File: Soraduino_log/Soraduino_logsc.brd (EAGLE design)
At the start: 27.4 x 29.5 mm, 26 parts, among them IC1 ATMEGA168-AU, IC2 LM1117IMPX-3.3, IC3 LM1117MPX-5.0

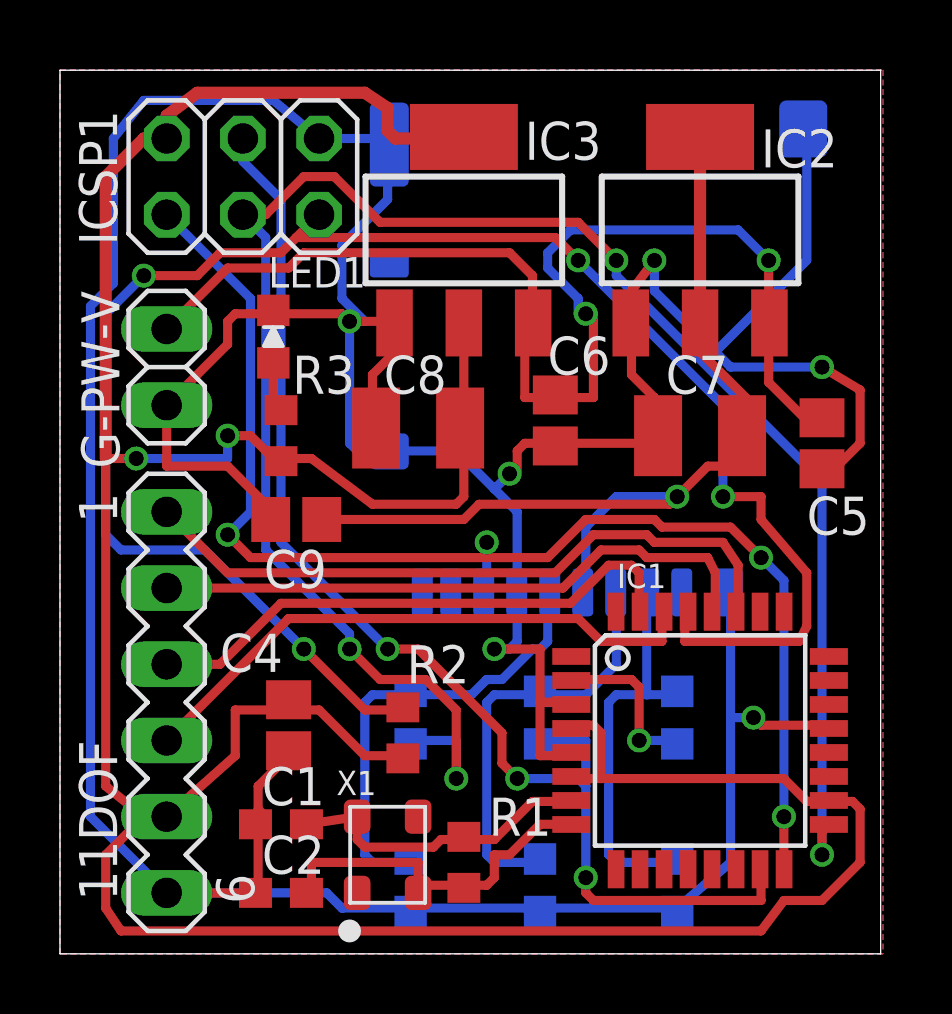
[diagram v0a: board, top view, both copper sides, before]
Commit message: fix I2C port mistake about sch
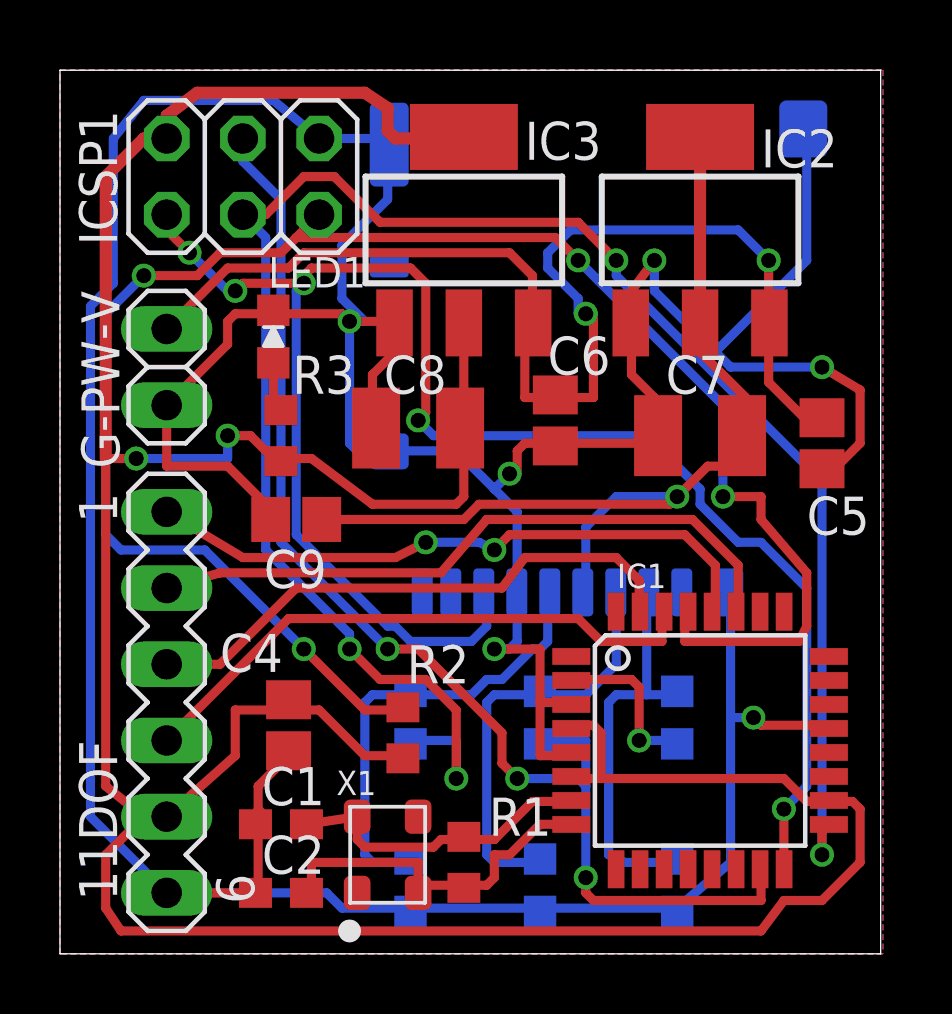
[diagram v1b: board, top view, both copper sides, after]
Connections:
- removed net N$9: 11DOF.2, IC1.28
- new net N$3: 11DOF.1, IC1.28
- net N$8: now also 11DOF.2; no longer 11DOF.1
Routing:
- net N$3: track 0.00 -> 21.2 mm, vias 0 -> 2
- net N$9: track 20.6 -> 0.00 mm
- net N$15: track 44.2 -> 58.4 mm, vias 4 -> 5
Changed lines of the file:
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@@
 <?xml version="1.0" encoding="utf-8"?>
 <!DOCTYPE eagle SYSTEM "eagle.dtd">
-<eagle version="6.4">
+<eagle version="6.5.0">
 <drawing>
 <settings>
@@
 <signal name="N$8">
 <contactref element="IC1" pad="27"/>
-<contactref element="11DOF" pad="1"/>
+<contactref element="11DOF" pad="2"/>
 <wire x1="22.606" y1="12.954" x2="22.606" y2="11.43" width="0.3048" layer="1"/>
-<wire x1="22.098" y1="13.716" x2="22.606" y2="12.954" width="0.3048" layer="1"/>
-<wire x1="19.812" y1="13.716" x2="22.098" y2="13.716" width="0.3048" layer="1"/>
-<wire x1="19.558" y1="13.97" x2="19.812" y2="13.716" width="0.3048" layer="1"/>
-<wire x1="17.78" y1="13.97" x2="19.558" y2="13.97" width="0.3048" layer="1"/>
-<wire x1="16.51" y1="12.7" x2="17.78" y2="13.97" width="0.3048" layer="1"/>
-<wire x1="5.588" y1="12.7" x2="16.51" y2="12.7" width="0.3048" layer="1"/>
-<wire x1="3.556" y1="14.732" x2="5.588" y2="12.7" width="0.3048" layer="1"/>
+<wire x1="21.082" y1="14.478" x2="22.606" y2="12.954" width="0.3048" layer="1"/>
+<wire x1="14.224" y1="14.478" x2="21.082" y2="14.478" width="0.3048" layer="1"/>
+<wire x1="12.7" y1="12.7" x2="14.224" y2="14.478" width="0.3048" layer="1"/>
+<wire x1="5.334" y1="12.7" x2="12.7" y2="12.7" width="0.3048" layer="1"/>
+<wire x1="3.556" y1="12.192" x2="5.334" y2="12.7" width="0.3048" layer="1"/>
 <wire x1="22.606" y1="11.43" x2="22.536" y2="11.4046" width="0.3048" layer="1"/>
-</signal>
-<signal name="N$9">
-<contactref element="IC1" pad="28"/>
-<contactref element="11DOF" pad="2"/>
-<wire x1="21.844" y1="12.7" x2="21.844" y2="11.43" width="0.3048" layer="1"/>
-<wire x1="21.59" y1="13.208" x2="21.844" y2="12.7" width="0.3048" layer="1"/>
-<wire x1="19.558" y1="13.208" x2="21.59" y2="13.208" width="0.3048" layer="1"/>
-<wire x1="19.304" y1="13.462" x2="19.558" y2="13.208" width="0.3048" layer="1"/>
-<wire x1="18.034" y1="13.462" x2="19.304" y2="13.462" width="0.3048" layer="1"/>
-<wire x1="16.764" y1="12.192" x2="18.034" y2="13.462" width="0.3048" layer="1"/>
-<wire x1="3.556" y1="12.192" x2="16.764" y2="12.192" width="0.3048" layer="1"/>
-<wire x1="21.844" y1="11.43" x2="21.736" y2="11.4046" width="0.3048" layer="1"/>
 </signal>
 <signal name="+5V">
@@
 <contactref element="U$1" pad="7"/>
 <contactref element="ICSP1" pad="1"/>
-<wire x1="24.13" y1="4.572" x2="24.13" y2="3.048" width="0.3048" layer="1"/>
-<wire x1="24.13" y1="12.446" x2="24.13" y2="4.572" width="0.3048" layer="16"/>
-<wire x1="23.368" y1="13.208" x2="24.13" y2="12.446" width="0.3048" layer="16"/>
-<wire x1="22.352" y1="14.224" x2="23.368" y2="13.208" width="0.3048" layer="1"/>
-<wire x1="20.066" y1="14.224" x2="22.352" y2="14.224" width="0.3048" layer="1"/>
-<wire x1="19.812" y1="14.478" x2="20.066" y2="14.224" width="0.3048" layer="1"/>
-<wire x1="17.526" y1="14.478" x2="19.812" y2="14.478" width="0.3048" layer="1"/>
-<wire x1="16.256" y1="13.208" x2="17.526" y2="14.478" width="0.3048" layer="1"/>
-<wire x1="6.35" y1="13.208" x2="14.224" y2="13.208" width="0.3048" layer="1"/>
-<wire x1="14.224" y1="13.208" x2="16.256" y2="13.208" width="0.3048" layer="1"/>
-<wire x1="5.588" y1="13.97" x2="6.35" y2="13.208" width="0.3048" layer="1"/>
-<wire x1="6.35" y1="14.732" x2="5.588" y2="13.97" width="0.3048" layer="16"/>
-<wire x1="6.35" y1="21.844" x2="6.35" y2="14.732" width="0.3048" layer="16"/>
-<wire x1="3.556" y1="24.638" x2="6.35" y2="21.844" width="0.3048" layer="16"/>
+<wire x1="3.556" y1="24.13" x2="3.556" y2="24.638" width="0.3048" layer="1"/>
+<wire x1="4.318" y1="23.368" x2="3.556" y2="24.13" width="0.3048" layer="1"/>
+<wire x1="5.588" y1="22.098" x2="4.318" y2="23.368" width="0.3048" layer="16"/>
+<wire x1="5.842" y1="22.098" x2="5.588" y2="22.098" width="0.3048" layer="16"/>
+<wire x1="6.096" y1="22.352" x2="5.842" y2="22.098" width="0.3048" layer="1"/>
+<wire x1="7.874" y1="22.352" x2="6.096" y2="22.352" width="0.3048" layer="1"/>
+<wire x1="8.382" y1="22.86" x2="7.874" y2="22.352" width="0.3048" layer="1"/>
+<wire x1="11.684" y1="22.86" x2="8.382" y2="22.86" width="0.3048" layer="1"/>
+<wire x1="12.192" y1="22.352" x2="11.684" y2="22.86" width="0.3048" layer="1"/>
+<wire x1="12.192" y1="18.034" x2="12.192" y2="22.352" width="0.3048" layer="1"/>
+<wire x1="11.938" y1="17.78" x2="12.192" y2="18.034" width="0.3048" layer="1"/>
+<wire x1="12.446" y1="17.272" x2="11.938" y2="17.78" width="0.3048" layer="16"/>
+<wire x1="19.558" y1="17.272" x2="12.446" y2="17.272" width="0.3048" layer="16"/>
+<wire x1="21.336" y1="15.494" x2="19.558" y2="17.272" width="0.3048" layer="16"/>
+<wire x1="21.336" y1="14.986" x2="21.336" y2="15.494" width="0.3048" layer="16"/>
+<wire x1="22.606" y1="13.716" x2="21.336" y2="14.986" width="0.3048" layer="16"/>
+<wire x1="23.368" y1="13.716" x2="22.606" y2="13.716" width="0.3048" layer="16"/>
+<wire x1="24.892" y1="12.192" x2="23.368" y2="13.716" width="0.3048" layer="16"/>
+<wire x1="24.892" y1="5.588" x2="24.892" y2="12.192" width="0.3048" layer="16"/>
+<wire x1="24.13" y1="4.826" x2="24.892" y2="5.588" width="0.3048" layer="16"/>
+<wire x1="24.13" y1="3.048" x2="24.13" y2="4.826" width="0.3048" layer="1"/>
 <wire x1="24.13" y1="3.048" x2="24.136" y2="2.8194" width="0.3048" layer="1"/>
-<via x="24.13" y="4.572" extent="1-16" drill="0.5" diameter="0.3048"/>
-<via x="23.368" y="13.208" extent="1-16" drill="0.5" diameter="0.3048"/>
-<via x="5.588" y="13.97" extent="1-16" drill="0.5" diameter="0.3048"/>
-<wire x1="14.224" y1="13.716" x2="14.224" y2="13.208" width="0.3048" layer="1"/>
-<wire x1="14.224" y1="12.192" x2="14.224" y2="13.716" width="0.3048" layer="16"/>
-<wire x1="14.224" y1="12.192" x2="14.126" y2="12.048" width="0.3048" layer="16"/>
-<via x="14.224" y="13.716" extent="1-16" drill="0.5" diameter="0.3048"/>
+<via x="4.318" y="23.368" extent="1-16" drill="0.5"/>
+<via x="5.842" y="22.098" extent="1-16" drill="0.5"/>
+<via x="11.938" y="17.78" extent="1-16" drill="0.5"/>
+<via x="24.13" y="4.826" extent="1-16" drill="0.5"/>
+<wire x1="14.224" y1="10.922" x2="14.224" y2="11.938" width="0.3048" layer="16"/>
+<wire x1="13.716" y1="10.414" x2="14.224" y2="10.922" width="0.3048" layer="16"/>
+<wire x1="11.684" y1="10.414" x2="13.716" y2="10.414" width="0.3048" layer="16"/>
+<wire x1="11.176" y1="10.922" x2="11.684" y2="10.414" width="0.3048" layer="16"/>
+<wire x1="10.922" y1="10.922" x2="11.176" y2="10.922" width="0.3048" layer="16"/>
+<wire x1="7.874" y1="13.97" x2="10.922" y2="10.922" width="0.3048" layer="16"/>
+<wire x1="7.874" y1="22.098" x2="7.874" y2="13.97" width="0.3048" layer="16"/>
+<wire x1="8.128" y1="22.352" x2="7.874" y2="22.098" width="0.3048" layer="16"/>
+<wire x1="7.874" y1="22.352" x2="8.128" y2="22.352" width="0.3048" layer="1"/>
+<wire x1="14.224" y1="11.938" x2="14.126" y2="12.048" width="0.3048" layer="16"/>
+<via x="8.128" y="22.352" extent="1-16" drill="0.5"/>
 </signal>
 <signal name="N$11">
@@
 <contactref element="IC1" pad="31"/>
 <contactref element="11DOF" pad="3"/>
-<wire x1="19.304" y1="12.7" x2="19.304" y2="11.43" width="0.3048" layer="1"/>
-<wire x1="19.05" y1="12.954" x2="19.304" y2="12.7" width="0.3048" layer="1"/>
-<wire x1="18.288" y1="12.954" x2="19.05" y2="12.954" width="0.3048" layer="1"/>
-<wire x1="17.018" y1="11.684" x2="18.288" y2="12.954" width="0.3048" layer="1"/>
-<wire x1="7.366" y1="11.684" x2="17.018" y2="11.684" width="0.3048" layer="1"/>
-<wire x1="5.334" y1="9.652" x2="7.366" y2="11.684" width="0.3048" layer="1"/>
+<wire x1="5.334" y1="9.652" x2="7.874" y2="12.192" width="0.3048" layer="1"/>
 <wire x1="3.556" y1="9.652" x2="5.334" y2="9.652" width="0.3048" layer="1"/>
+<wire x1="14.732" y1="12.192" x2="7.874" y2="12.192" width="0.3048" layer="1"/>
+<wire x1="15.494" y1="13.208" x2="14.732" y2="12.192" width="0.3048" layer="1"/>
+<wire x1="18.542" y1="13.208" x2="15.494" y2="13.208" width="0.3048" layer="1"/>
+<wire x1="19.304" y1="11.43" x2="19.304" y2="12.446" width="0.3048" layer="1"/>
+<wire x1="19.304" y1="12.446" x2="18.542" y2="13.208" width="0.3048" layer="1"/>
 <wire x1="19.304" y1="11.43" x2="19.336" y2="11.4046" width="0.3048" layer="1"/>
 </signal>
+<signal name="N$3">
+<contactref element="IC1" pad="28"/>
+<contactref element="11DOF" pad="1"/>
+<wire x1="21.844" y1="12.954" x2="21.844" y2="11.43" width="0.3048" layer="1"/>
+<wire x1="20.828" y1="13.97" x2="21.844" y2="12.954" width="0.3048" layer="1"/>
+<wire x1="14.986" y1="13.97" x2="20.828" y2="13.97" width="0.3048" layer="1"/>
+<wire x1="14.478" y1="13.462" x2="14.986" y2="13.97" width="0.3048" layer="1"/>
+<wire x1="13.97" y1="13.716" x2="14.478" y2="13.462" width="0.3048" layer="16"/>
+<wire x1="12.192" y1="13.716" x2="13.97" y2="13.716" width="0.3048" layer="16"/>
+<wire x1="11.176" y1="13.208" x2="12.192" y2="13.716" width="0.3048" layer="1"/>
+<wire x1="6.096" y1="13.208" x2="11.176" y2="13.208" width="0.3048" layer="1"/>
+<wire x1="3.556" y1="14.732" x2="6.096" y2="13.208" width="0.3048" layer="1"/>
+<wire x1="21.844" y1="11.43" x2="21.736" y2="11.4046" width="0.3048" layer="1"/>
+<via x="14.478" y="13.462" extent="1-16" drill="0.5"/>
+<via x="12.192" y="13.716" extent="1-16" drill="0.5"/>
+</signal>
 </signals>
